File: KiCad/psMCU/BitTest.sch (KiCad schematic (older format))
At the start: 40 parts

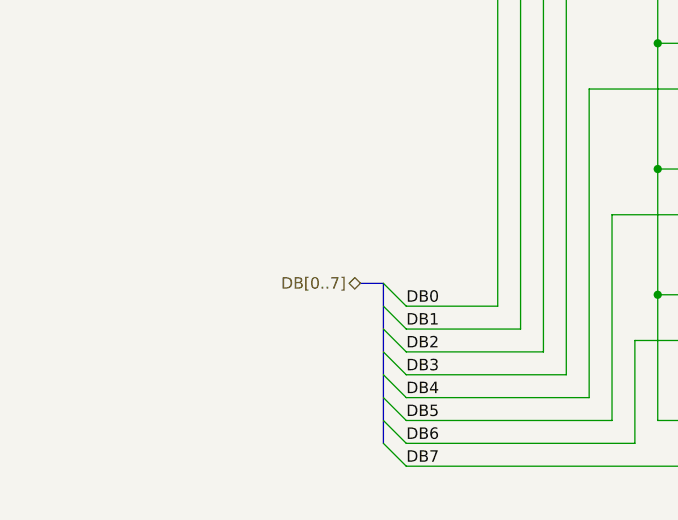
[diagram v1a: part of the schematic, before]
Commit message: First ERC pass
    All unconnects solved, need to inspect Tristate errors.
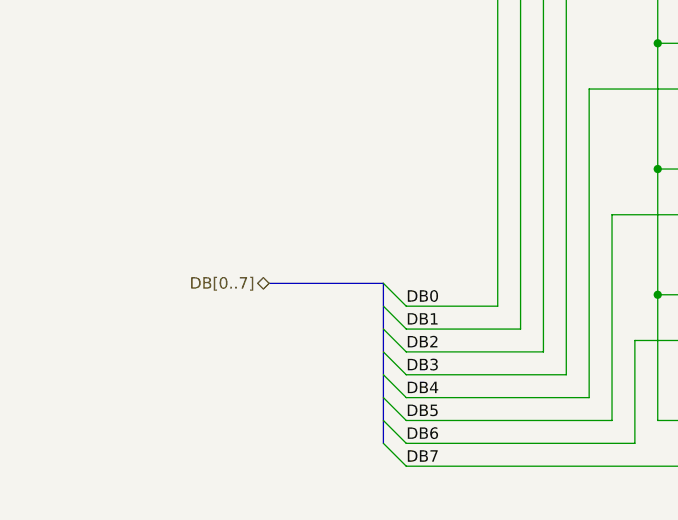
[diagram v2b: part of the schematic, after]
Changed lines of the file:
@@
 $Descr A4 11693 8268
 encoding utf-8
-Sheet 154 209
+Sheet 84 207
 Title "psMCU"
 Date ""
@@
 DB7
 Wire Bus Line
-	2050 5850 1950 5850
-Text HLabel 1950 5850 0    50   3State ~ 0
+	2050 5850 1550 5850
+Text HLabel 1550 5850 0    50   3State ~ 0
 DB[0..7]
 Entry Wire Line

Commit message: Added some footprints, small optimisations
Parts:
- U?: footprint (none) -> Package_TO_SOT_SMD:SOT-353_SC-70-5
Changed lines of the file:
@@
 F 0 "U?" H 2050 2350 50  0000 C CNN
 F 1 "74LVC1G04" H 2200 2450 50  0000 C CNN
-F 2 "" H 1950 2550 50  0001 C CNN
+F 2 "Package_TO_SOT_SMD:SOT-353_SC-70-5" H 1950 2550 50  0001 C CNN
 F 3 "http://www.ti.com/lit/sg/scyt129e/scyt129e.pdf" H 1950 2550 50  0001 C CNN
 	1    1950 2550

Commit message: Started some documentation work.
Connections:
- net labels removed: Inst0, Inst1, Inst13, Inst14, Inst15, Inst2, Inst3, Inst4, Inst5, Inst6, Inst7, Inst8
- wire segments 179 -> 167
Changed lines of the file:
@@
 $Descr A4 11693 8268
 encoding utf-8
-Sheet 84 202
+Sheet 77 202
 Title "psMCU"
 Date ""
@@
 	8600 4700 8450 4700
 Entry Wire Line
-	1100 800  1200 900
-Entry Wire Line
-	1100 900  1200 1000
-Entry Wire Line
-	1100 1000 1200 1100
-Entry Wire Line
-	1100 1100 1200 1200
-Entry Wire Line
-	1100 1200 1200 1300
-Entry Wire Line
-	1100 1300 1200 1400
-Entry Wire Line
-	1100 1400 1200 1500
-Entry Wire Line
-	1100 1500 1200 1600
-Wire Bus Line
-	1100 750  1050 750
-Entry Wire Line
-	1100 2300 1200 2400
-Entry Wire Line
-	1100 2200 1200 2300
-Entry Wire Line
-	1100 2100 1200 2200
-Entry Wire Line
 	1100 2000 1200 2100
 Entry Wire Line
@@
 Entry Wire Line
 	1100 1800 1200 1900
-Entry Wire Line
-	1100 1700 1200 1800
-Entry Wire Line
-	1100 1600 1200 1700
-Wire Wire Line
-	1200 1700 1450 1700
-Wire Wire Line
-	1200 2200 1450 2200
-Wire Wire Line
-	1200 2300 1450 2300
-Wire Wire Line
-	1200 2400 1450 2400
-Text HLabel 1050 750  0    50   Input ~ 0
+Text HLabel 1000 1550 0    50   Input ~ 0
 Inst[0..15]
-Entry Wire Line
-	1100 800  1200 900
-Entry Wire Line
-	1100 900  1200 1000
-Entry Wire Line
-	1100 1000 1200 1100
-Entry Wire Line
-	1100 1100 1200 1200
-Entry Wire Line
-	1100 1200 1200 1300
-Entry Wire Line
-	1100 1300 1200 1400
-Entry Wire Line
-	1100 1400 1200 1500
-Entry Wire Line
-	1100 1500 1200 1600
-Text Label 1200 900  0    50   ~ 0
-Inst0
-Text Label 1200 1000 0    50   ~ 0
-Inst1
-Text Label 1200 1100 0    50   ~ 0
-Inst2
-Text Label 1200 1200 0    50   ~ 0
-Inst3
-Text Label 1200 1300 0    50   ~ 0
-Inst4
-Text Label 1200 1400 0    50   ~ 0
-Inst5
-Text Label 1200 1500 0    50   ~ 0
-Inst6
-Text Label 1200 1600 0    50   ~ 0
-Inst7
-Text Label 1200 2400 0    50   ~ 0
-Inst15
-Text Label 1200 2300 0    50   ~ 0
-Inst14
-Text Label 1200 2200 0    50   ~ 0
-Inst13
 Text Label 1200 2100 0    50   ~ 0
 Inst12
@@
 Text Label 1200 1900 0    50   ~ 0
 Inst10
-Text Label 1200 1800 0    50   ~ 0
-Inst9
-Text Label 1200 1700 0    50   ~ 0
-Inst8
-Entry Wire Line
-	1100 2300 1200 2400
-Entry Wire Line
-	1100 2200 1200 2300
-Entry Wire Line
-	1100 2100 1200 2200
 Entry Wire Line
 	1100 2000 1200 2100
@@
 Entry Wire Line
 	1100 1800 1200 1900
-Entry Wire Line
-	1100 1700 1200 1800
-Entry Wire Line
-	1100 1600 1200 1700
-Wire Wire Line
-	1200 1600 1450 1600
-Wire Wire Line
-	1200 1500 1450 1500
-Wire Wire Line
-	1200 1400 1450 1400
-Wire Wire Line
-	1200 1300 1450 1300
-Wire Wire Line
-	1200 1200 1450 1200
-Wire Wire Line
-	1200 1100 1450 1100
-Wire Wire Line
-	1200 1000 1450 1000
-Wire Wire Line
-	1200 900  1450 900
 Wire Wire Line
 	1200 1800 3350 1800
@@
 Wire Wire Line
 	2550 2750 3350 2750
+Entry Wire Line
+	1100 1700 1200 1800
+Entry Wire Line
+	1100 1700 1200 1800
+Text Label 1200 1800 0    50   ~ 0
+Inst9
+Wire Bus Line
+	1000 1550 1100 1550
+Wire Bus Line
+	1100 1550 1100 2000
 Wire Bus Line
 	2050 5850 2050 6550
-Wire Bus Line
-	1100 750  1100 2300
 $EndSCHEMATC

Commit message: First Schematic Draft done.
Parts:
- removed C? (x8): 0u1, Capacitor_SMD:C_0603_1608Metric, symbol Device:C_Small
- removed U?: 74HC238, symbol 74xx_IEEE:74HC238
- removed U? (x10): 74HC08, symbol 74xx:74LS08
- removed U? (x10): 74HC32, symbol 74xx:74LS32
- removed U? (x10): 74HC86, symbol 74xx:74HC86
- removed U?: 74LVC1G04, Package_TO_SOT_SMD:SOT-353_SC-70-5, symbol 74xGxx:74LVC1G04
- added C176, C177: 0u1, NoRef_Footprints:C_0603_1608Metric_NoRef, symbol Device:C_Small
- added D177: Bit[0], NoRef_Footprints:D_0603_1608Metric_NoRef, symbol Device:LED_Small
- added D178: Bit[1], NoRef_Footprints:D_0603_1608Metric_NoRef, symbol Device:LED_Small
- added D179: Bit[2], NoRef_Footprints:D_0603_1608Metric_NoRef, symbol Device:LED_Small
- added D180: Test for 1, NoRef_Footprints:D_0603_1608Metric_NoRef, symbol Device:LED_Small
- added D181: Test for 0, NoRef_Footprints:D_0603_1608Metric_NoRef, symbol Device:LED_Small
- added D182: BitTest Result, NoRef_Footprints:D_0603_1608Metric_NoRef, symbol Device:LED_Small
- added R182, R183, R184, R185, R186: rled, NoRef_Footprints:R_0603_1608Metric, symbol Device:R_Small
- added U176: 74HC251, symbol 74xx:74LS251
- added U177: 74LVC1G157, Package_TO_SOT_SMD:SOT-363_SC-70-6, symbol 74LVC1G157:74LVC1G157
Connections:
- net +5V: now also C176.2, C177.2, U176.16 (VCC), U176.7 (~OE), U177.5 (Vcc)
- net CNDT_AFFIRMATIVE: now also R186.2, U177.4 (Y)
- net DB0: now also U176.4 (I0)
- net DB1: now also U176.3 (I1)
- net DB2: now also U176.2 (I2)
- net DB3: now also U176.1 (I3)
- net DB4: now also U176.15 (I4)
- net DB5: now also U176.14 (I5)
- net DB6: now also U176.13 (I6)
- net DB7: now also U176.12 (I7)
- net GND: now also C176.1, C177.1, D177.1 (K), D178.1 (K), D179.1 (K), D180.1 (K), D181.2 (A), D182.1 (K), U176.8 (GND), U177.2 (GND)
- net Inst10: now also R183.2, U176.10 (S1)
- net Inst11: now also R184.2, U176.9 (S2)
- net Inst12: now also R185.2, U177.6 (S)
- net Inst9: now also R182.2, U176.11 (S0)
- new net: U176.5 (Y), U177.1 (I1)
- new net: U176.6 (~Y), U177.3 (I0)
- new net: D182.2 (A), R186.1
- new net: D180.2 (A), D181.1 (K), R185.1
- new net: D177.2 (A), R182.1
- new net: D178.2 (A), R183.1
- new net: D179.2 (A), R184.1
- no-connect marks 1 -> 0

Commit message: Small improvements.
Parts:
- renumbered C176 to C174, C177 to C175, U176 to U174, U177 to U175
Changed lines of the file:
@@
 	2950 2850 3100 2850
 $Comp
-L 74xx:74LS251 U176
+L 74xx:74LS251 U174
 U 1 1 6198D1E4
 P 5300 2650
-F 0 "U176" H 5450 3500 50  0000 C CNN
+F 0 "U174" H 5450 3500 50  0000 C CNN
 F 1 "74HC251" H 5550 3400 50  0000 C CNN
 F 2 "" H 5300 2650 50  0001 C CNN
@@
 AR Path="/608BF85D/6199CA3D" Ref="#PWR?"  Part="1"
 AR Path="/608BF85D/5FFAAF6D/6199CA3D" Ref="#PWR?"  Part="1"
-AR Path="/5FD6B1FB/6199CA3D" Ref="#PWR0787"  Part="1"
-F 0 "#PWR0787" H 6950 2300 50  0001 C CNN
+AR Path="/5FD6B1FB/6199CA3D" Ref="#PWR0772"  Part="1"
+F 0 "#PWR0772" H 6950 2300 50  0001 C CNN
 F 1 "GND" V 6955 2422 50  0000 R CNN
 F 2 "" H 6950 2550 50  0001 C CNN
@@
 AR Path="/608BF85D/6199CA33" Ref="#PWR?"  Part="1"
 AR Path="/608BF85D/5FFAAF6D/6199CA33" Ref="#PWR?"  Part="1"
-AR Path="/5FD6B1FB/6199CA33" Ref="#PWR0786"  Part="1"
-F 0 "#PWR0786" H 6950 1650 50  0001 C CNN
+AR Path="/5FD6B1FB/6199CA33" Ref="#PWR0771"  Part="1"
+F 0 "#PWR0771" H 6950 1650 50  0001 C CNN
 F 1 "+5V" H 7050 1900 50  0000 C CNN
 F 2 "" H 6950 1800 50  0001 C CNN
@@
 AR Path="/608BF85D/6199CA2D" Ref="C?"  Part="1"
 AR Path="/608BF85D/5FFAAF6D/6199CA2D" Ref="C?"  Part="1"
-AR Path="/5FD6B1FB/6199CA2D" Ref="C177"  Part="1"
-F 0 "C177" V 7200 1850 50  0000 C CNN
+AR Path="/5FD6B1FB/6199CA2D" Ref="C175"  Part="1"
+F 0 "C175" V 7200 1850 50  0000 C CNN
 F 1 "0u1" V 7200 2050 50  0000 C CNN
 F 2 "NoRef_Footprints:C_0603_1608Metric_NoRef" H 7100 1850 50  0001 C CNN
@@
 AR Path="/608BF85D/6199CA26" Ref="#PWR?"  Part="1"
 AR Path="/608BF85D/5FFAAF6D/6199CA26" Ref="#PWR?"  Part="1"
-AR Path="/5FD6B1FB/6199CA26" Ref="#PWR0788"  Part="1"
-F 0 "#PWR0788" H 7250 1600 50  0001 C CNN
+AR Path="/5FD6B1FB/6199CA26" Ref="#PWR0773"  Part="1"
+F 0 "#PWR0773" H 7250 1600 50  0001 C CNN
 F 1 "GND" V 7350 1850 50  0000 R CNN
 F 2 "" H 7250 1850 50  0001 C CNN
@@
 AR Path="/608BF85D/6199CA20" Ref="U?"  Part="1"
 AR Path="/608BF85D/5FFAAF6D/6199CA20" Ref="U?"  Part="1"
-AR Path="/5FD6B1FB/6199CA20" Ref="U177"  Part="1"
-F 0 "U177" H 7100 2000 50  0000 L CNN
+AR Path="/5FD6B1FB/6199CA20" Ref="U175"  Part="1"
+F 0 "U175" H 7100 2000 50  0000 L CNN
 F 1 "74LVC1G157" V 7050 1550 50  0000 L CNN
 F 2 "Package_TO_SOT_SMD:SOT-363_SC-70-6" H 6600 1625 50  0001 C CNN
@@
 AR Path="/608BF85D/619DF268" Ref="#PWR?"  Part="1"
 AR Path="/608BF85D/5FFAAF6D/619DF268" Ref="#PWR?"  Part="1"
-AR Path="/5FD6B1FB/619DF268" Ref="#PWR0782"  Part="1"
-F 0 "#PWR0782" H 5300 1400 50  0001 C CNN
+AR Path="/5FD6B1FB/619DF268" Ref="#PWR0767"  Part="1"
+F 0 "#PWR0767" H 5300 1400 50  0001 C CNN
 F 1 "+5V" H 5400 1650 50  0000 C CNN
 F 2 "" H 5300 1550 50  0001 C CNN
@@
 AR Path="/608BF85D/619DF26E" Ref="C?"  Part="1"
 AR Path="/608BF85D/5FFAAF6D/619DF26E" Ref="C?"  Part="1"
-AR Path="/5FD6B1FB/619DF26E" Ref="C176"  Part="1"
-F 0 "C176" V 5550 1600 50  0000 C CNN
+AR Path="/5FD6B1FB/619DF26E" Ref="C174"  Part="1"
+F 0 "C174" V 5550 1600 50  0000 C CNN
 F 1 "0u1" V 5550 1800 50  0000 C CNN
 F 2 "NoRef_Footprints:C_0603_1608Metric_NoRef" H 5450 1600 50  0001 C CNN
@@
 AR Path="/608BF85D/619DF275" Ref="#PWR?"  Part="1"
 AR Path="/608BF85D/5FFAAF6D/619DF275" Ref="#PWR?"  Part="1"
-AR Path="/5FD6B1FB/619DF275" Ref="#PWR0784"  Part="1"
-F 0 "#PWR0784" H 5600 1350 50  0001 C CNN
+AR Path="/5FD6B1FB/619DF275" Ref="#PWR0769"  Part="1"
+F 0 "#PWR0769" H 5600 1350 50  0001 C CNN
 F 1 "GND" V 5700 1600 50  0000 R CNN
 F 2 "" H 5600 1600 50  0001 C CNN
@@
 AR Path="/608BF85D/61A283F6" Ref="#PWR?"  Part="1"
 AR Path="/608BF85D/5FFAAF6D/61A283F6" Ref="#PWR?"  Part="1"
-AR Path="/5FD6B1FB/61A283F6" Ref="#PWR0778"  Part="1"
-F 0 "#PWR0778" H 4700 3200 50  0001 C CNN
+AR Path="/5FD6B1FB/61A283F6" Ref="#PWR0763"  Part="1"
+F 0 "#PWR0763" H 4700 3200 50  0001 C CNN
 F 1 "+5V" V 4700 3550 50  0000 C CNN
 F 2 "" H 4700 3350 50  0001 C CNN
@@
 AR Path="/608BF85D/61A29CCC" Ref="#PWR?"  Part="1"
 AR Path="/608BF85D/5FFAAF6D/61A29CCC" Ref="#PWR?"  Part="1"
-AR Path="/5FD6B1FB/61A29CCC" Ref="#PWR0783"  Part="1"
-F 0 "#PWR0783" H 5300 3450 50  0001 C CNN
+AR Path="/5FD6B1FB/61A29CCC" Ref="#PWR0768"  Part="1"
+F 0 "#PWR0768" H 5300 3450 50  0001 C CNN
 F 1 "GND" H 5305 3527 50  0000 C CNN
 F 2 "" H 5300 3700 50  0001 C CNN
@@
 AR Path="/5FD65308/605425EC/61A54D1A" Ref="#PWR?"  Part="1"
 AR Path="/5F43204F/61A54D1A" Ref="#PWR?"  Part="1"
-AR Path="/5FD6B1FB/61A54D1A" Ref="#PWR0789"  Part="1"
-F 0 "#PWR0789" H 8700 2450 50  0001 C CNN
+AR Path="/5FD6B1FB/61A54D1A" Ref="#PWR0774"  Part="1"
+F 0 "#PWR0774" H 8700 2450 50  0001 C CNN
 F 1 "GND" H 8705 2527 50  0000 C CNN
 F 2 "" H 8700 2700 50  0001 C CNN
@@
 AR Path="/5FD65308/605425EC/61A65FB8" Ref="#PWR?"  Part="1"
 AR Path="/5F43204F/61A65FB8" Ref="#PWR?"  Part="1"
-AR Path="/5FD6B1FB/61A65FB8" Ref="#PWR0785"  Part="1"
-F 0 "#PWR0785" H 6050 4700 50  0001 C CNN
+AR Path="/5FD6B1FB/61A65FB8" Ref="#PWR0770"  Part="1"
+F 0 "#PWR0770" H 6050 4700 50  0001 C CNN
 F 1 "GND" H 6055 4777 50  0000 C CNN
 F 2 "" H 6050 4950 50  0001 C CNN
@@
 AR Path="/5FD65308/605425EC/61A79E8B" Ref="#PWR?"  Part="1"
 AR Path="/5F43204F/61A79E8B" Ref="#PWR?"  Part="1"
-AR Path="/5FD6B1FB/61A79E8B" Ref="#PWR0779"  Part="1"
-F 0 "#PWR0779" H 5100 4800 50  0001 C CNN
+AR Path="/5FD6B1FB/61A79E8B" Ref="#PWR0764"  Part="1"
+F 0 "#PWR0764" H 5100 4800 50  0001 C CNN
 F 1 "GND" H 5105 4877 50  0000 C CNN
 F 2 "" H 5100 5050 50  0001 C CNN
@@
 AR Path="/5FD65308/605425EC/61A7D5F5" Ref="#PWR?"  Part="1"
 AR Path="/5F43204F/61A7D5F5" Ref="#PWR?"  Part="1"
-AR Path="/5FD6B1FB/61A7D5F5" Ref="#PWR0780"  Part="1"
-F 0 "#PWR0780" H 5100 5200 50  0001 C CNN
+AR Path="/5FD6B1FB/61A7D5F5" Ref="#PWR0765"  Part="1"
+F 0 "#PWR0765" H 5100 5200 50  0001 C CNN
 F 1 "GND" H 5105 5277 50  0000 C CNN
 F 2 "" H 5100 5450 50  0001 C CNN
@@
 AR Path="/5FD65308/605425EC/61A7EE22" Ref="#PWR?"  Part="1"
 AR Path="/5F43204F/61A7EE22" Ref="#PWR?"  Part="1"
-AR Path="/5FD6B1FB/61A7EE22" Ref="#PWR0781"  Part="1"
-F 0 "#PWR0781" H 5100 5600 50  0001 C CNN
+AR Path="/5FD6B1FB/61A7EE22" Ref="#PWR0766"  Part="1"
+F 0 "#PWR0766" H 5100 5600 50  0001 C CNN
 F 1 "GND" H 5105 5677 50  0000 C CNN
 F 2 "" H 5100 5850 50  0001 C CNN
